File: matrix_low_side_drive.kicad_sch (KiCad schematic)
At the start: 20 parts

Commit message: [#72133] Unify sheet size
Signed-off-by: Dawid Lentka <dlentka@antmicro.com>
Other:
- title: (none) -> LED Panel Board
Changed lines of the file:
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@@
 	(generator_version "8.0")
 	(paper "A4")
+	(title_block
+		(title "LED Panel Board")
+		(date "28.01.2025")
+		(rev "1.0.0")
+	)
 	(bus_entry
 		(at 121.92 30.48)

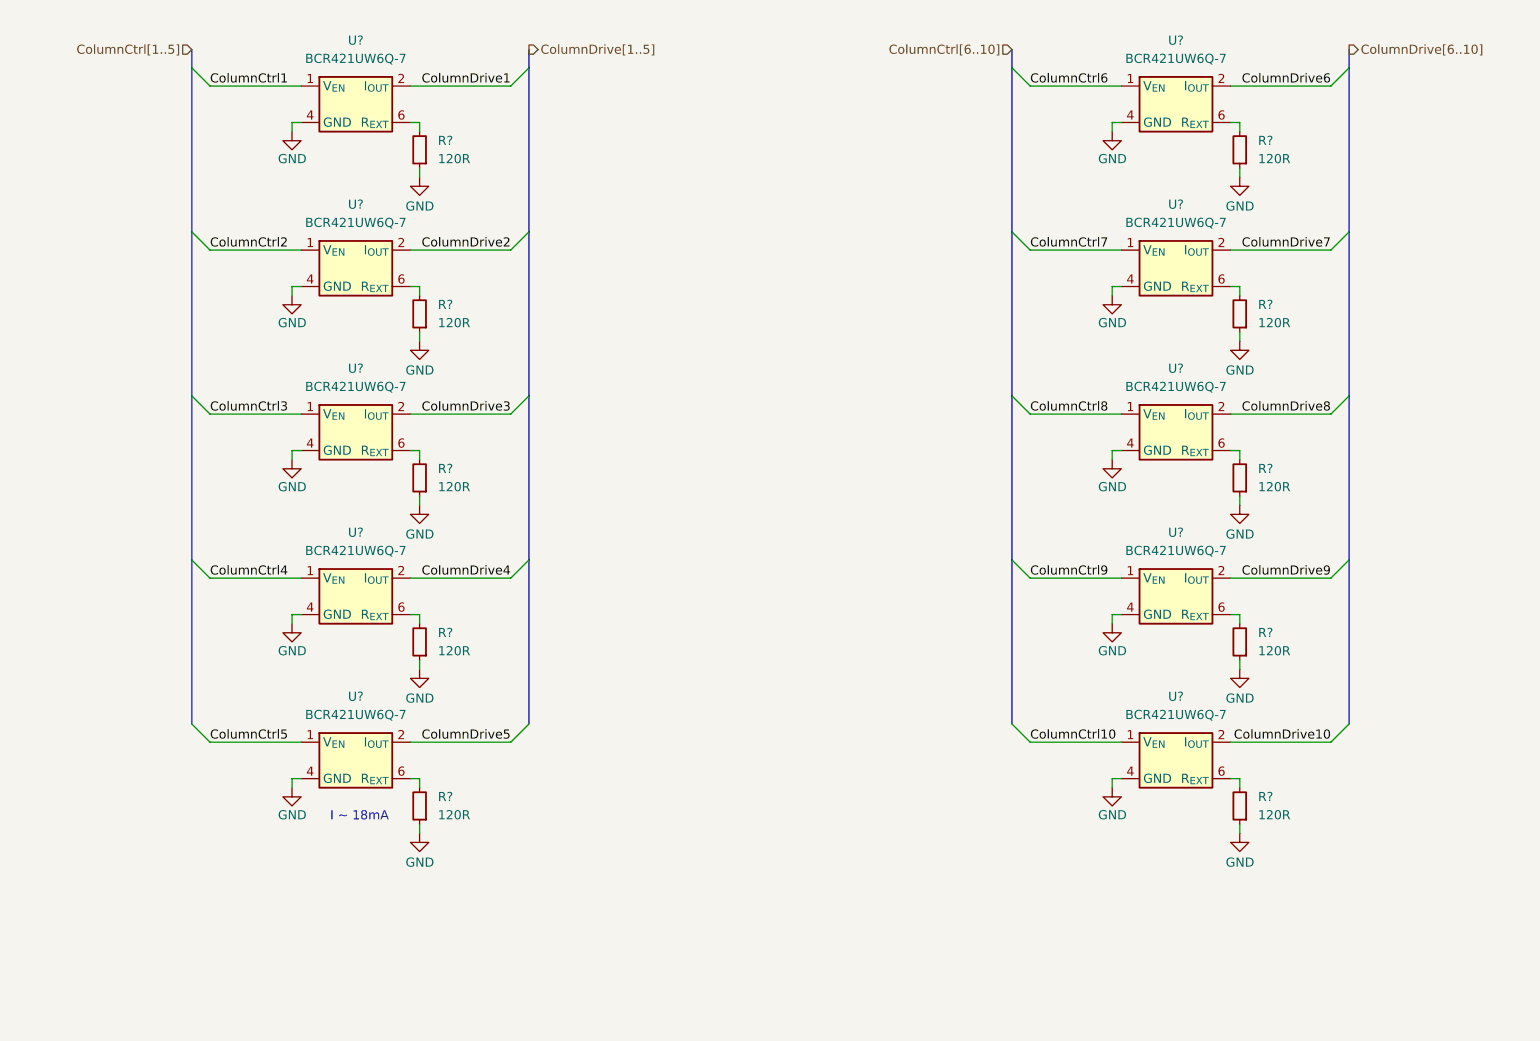
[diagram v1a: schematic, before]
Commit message: [#72133] Annotate schematics
Signed-off-by: Dawid Lentka <dlentka@antmicro.com>
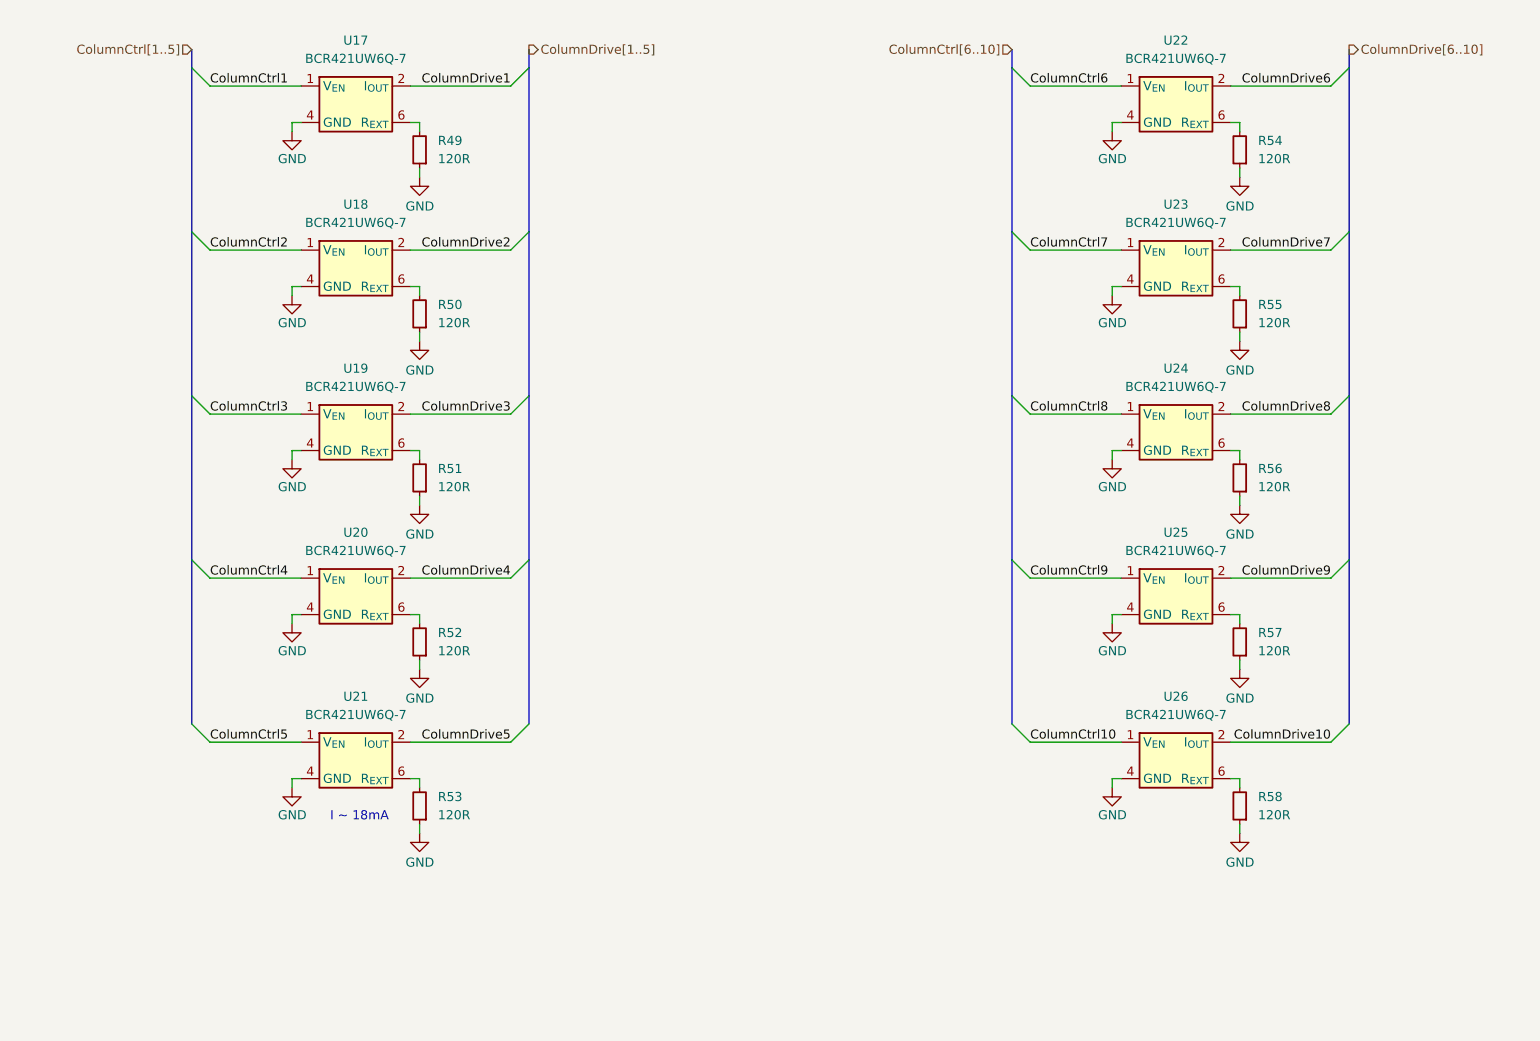
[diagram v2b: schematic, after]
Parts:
- gave numbers to parts that had none: 20

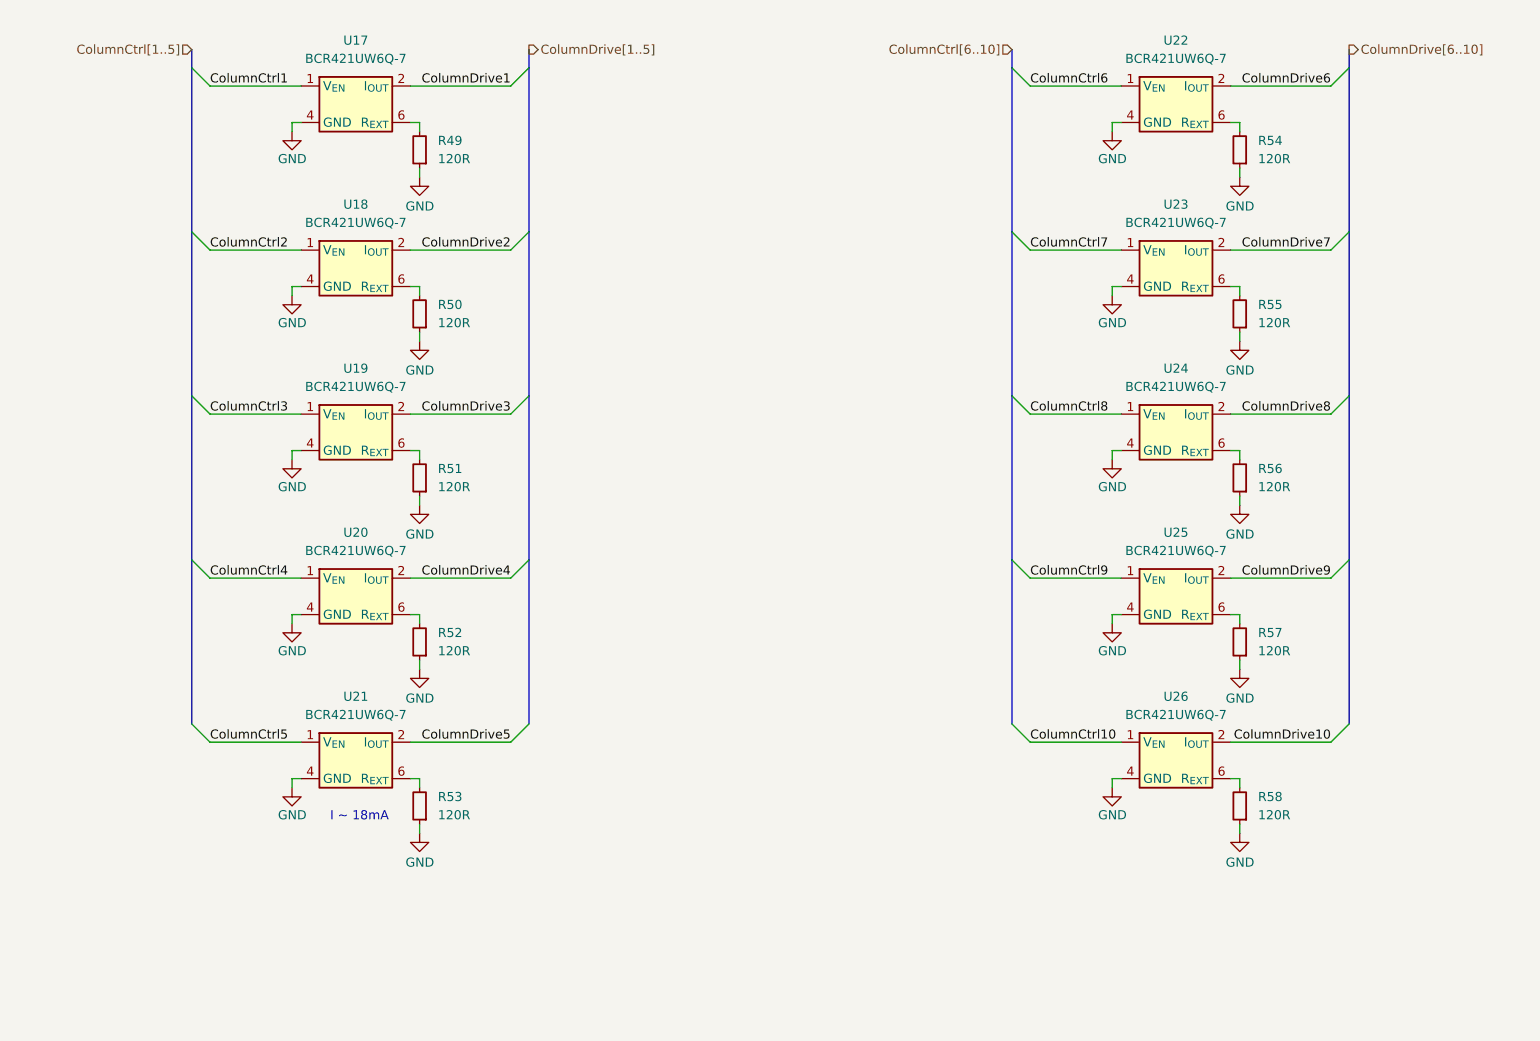
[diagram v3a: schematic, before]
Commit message: [#72133] Add captions to schematic sheets
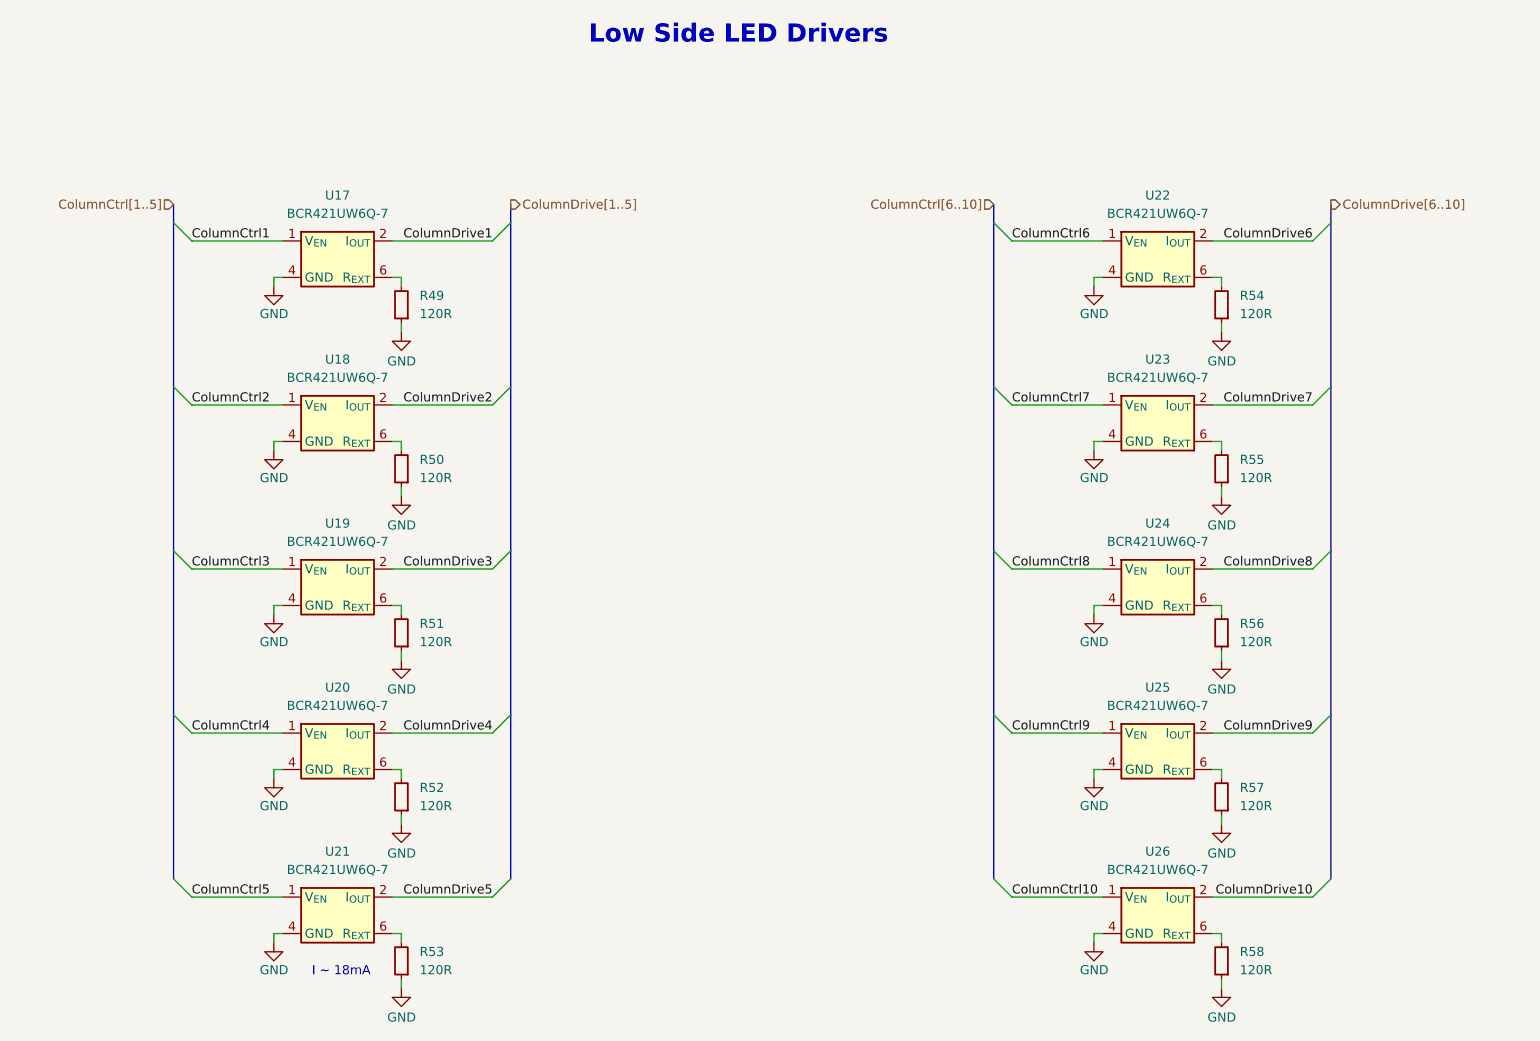
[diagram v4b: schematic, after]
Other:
- note added: "Low Side LED Drivers"
- moved on the sheet: R49, R50, R51, R52, R53, R54, R55, R56, R57, R58, U17, U18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
